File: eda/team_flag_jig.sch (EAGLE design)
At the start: 7 parts, among them J2 AVR_SPI_PRG_6PTH

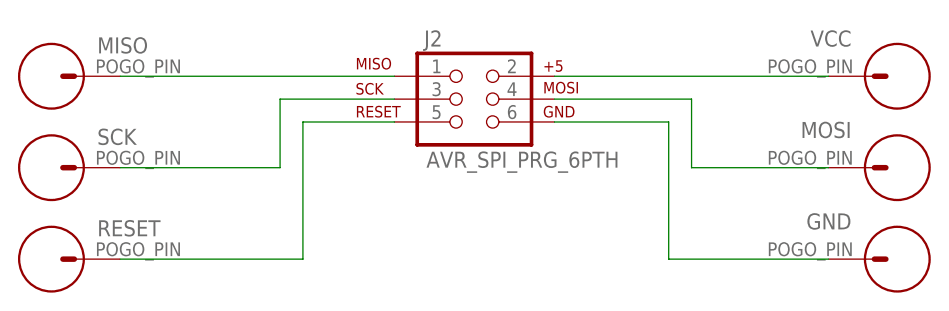
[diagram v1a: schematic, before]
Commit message: Ribboncable pinout fixed.
On battery_buzzer, smartsensor, and smartsensorPowered.
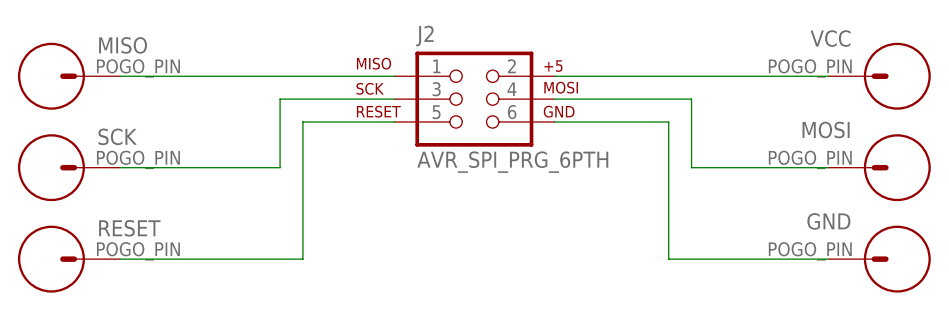
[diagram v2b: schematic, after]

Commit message: All jigs probe vias accessible after populating.
Also changed "VCC" signal name on jigs to "5V" to match boards.
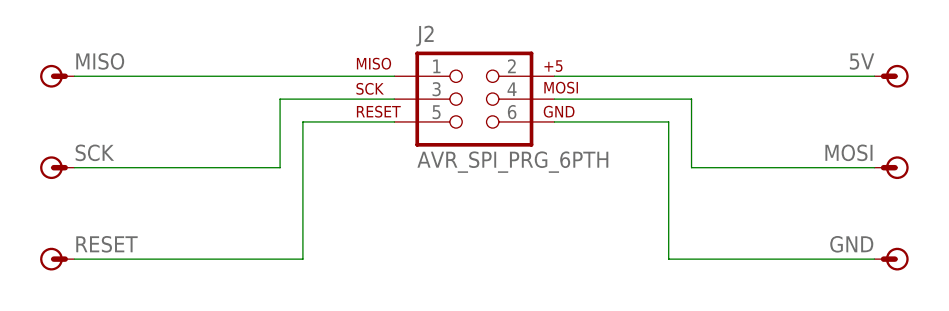
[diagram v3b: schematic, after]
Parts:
- renumbered VCC to 5V
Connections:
- net VCC renamed 5V
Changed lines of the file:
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@@
 <part name="SCK" library="pie" deviceset="POGO_PIN" device=""/>
 <part name="RESET" library="pie" deviceset="POGO_PIN" device=""/>
-<part name="VCC" library="pie" deviceset="POGO_PIN" device=""/>
+<part name="5V" library="pie" deviceset="POGO_PIN" device=""/>
 <part name="MOSI" library="pie" deviceset="POGO_PIN" device=""/>
 <part name="GND" library="pie" deviceset="POGO_PIN" device=""/>
@@
 </instance>
 <instance part="J2" gate="G$1" x="121.92" y="111.76"/>
-<instance part="MISO" gate="G$1" x="76.2" y="114.3"/>
-<instance part="SCK" gate="G$1" x="76.2" y="104.14"/>
-<instance part="RESET" gate="G$1" x="76.2" y="93.98"/>
-<instance part="VCC" gate="G$1" x="170.18" y="114.3" smashed="yes" rot="R180">
-<attribute name="NAME" x="165.1" y="119.38" size="1.778" layer="95" rot="R180"/>
+<instance part="MISO" gate="G$1" x="76.2" y="114.3" smashed="yes">
+<attribute name="VALUE" x="77.47" y="111.76" size="1.778" layer="96"/>
+<attribute name="NAME" x="78.74" y="115.062" size="1.778" layer="95"/>
+</instance>
+<instance part="SCK" gate="G$1" x="76.2" y="104.14" smashed="yes">
+<attribute name="VALUE" x="77.47" y="101.6" size="1.778" layer="96"/>
+<attribute name="NAME" x="78.74" y="104.902" size="1.778" layer="95"/>
+</instance>
+<instance part="RESET" gate="G$1" x="76.2" y="93.98" smashed="yes">
+<attribute name="VALUE" x="77.47" y="91.44" size="1.778" layer="96"/>
+<attribute name="NAME" x="78.74" y="94.742" size="1.778" layer="95"/>
+</instance>
+<instance part="5V" gate="G$1" x="170.18" y="114.3" smashed="yes" rot="R180">
+<attribute name="NAME" x="167.64" y="116.84" size="1.778" layer="95" rot="R180"/>
 <attribute name="VALUE" x="165.1" y="118.11" size="1.778" layer="96" rot="R180"/>
 </instance>
 <instance part="MOSI" gate="G$1" x="170.18" y="104.14" smashed="yes" rot="R180">
-<attribute name="NAME" x="165.1" y="109.22" size="1.778" layer="95" rot="R180"/>
+<attribute name="NAME" x="167.64" y="106.68" size="1.778" layer="95" rot="R180"/>
 <attribute name="VALUE" x="165.1" y="107.95" size="1.778" layer="96" rot="R180"/>
 </instance>
 <instance part="GND" gate="G$1" x="170.18" y="93.98" smashed="yes" rot="R180">
-<attribute name="NAME" x="165.1" y="99.06" size="1.778" layer="95" rot="R180"/>
+<attribute name="NAME" x="167.64" y="96.52" size="1.778" layer="95" rot="R180"/>
 <attribute name="VALUE" x="165.1" y="97.79" size="1.778" layer="96" rot="R180"/>
 </instance>
@@
 <wire x1="144.78" y1="109.22" x2="144.78" y2="93.98" width="0.1524" layer="91"/>
 <pinref part="GND" gate="G$1" pin="P$1"/>
-<wire x1="144.78" y1="93.98" x2="162.56" y2="93.98" width="0.1524" layer="91"/>
+<wire x1="144.78" y1="93.98" x2="167.64" y2="93.98" width="0.1524" layer="91"/>
 </segment>
 </net>
@@
 <wire x1="147.32" y1="111.76" x2="147.32" y2="104.14" width="0.1524" layer="91"/>
 <pinref part="MOSI" gate="G$1" pin="P$1"/>
-<wire x1="147.32" y1="104.14" x2="162.56" y2="104.14" width="0.1524" layer="91"/>
+<wire x1="147.32" y1="104.14" x2="167.64" y2="104.14" width="0.1524" layer="91"/>
 </segment>
 </net>
-<net name="VCC" class="0">
+<net name="5V" class="0">
 <segment>
 <pinref part="J2" gate="G$1" pin="2"/>
-<pinref part="VCC" gate="G$1" pin="P$1"/>
-<wire x1="132.08" y1="114.3" x2="162.56" y2="114.3" width="0.1524" layer="91"/>
+<pinref part="5V" gate="G$1" pin="P$1"/>
+<wire x1="132.08" y1="114.3" x2="167.64" y2="114.3" width="0.1524" layer="91"/>
 </segment>
 </net>
@@
 <wire x1="104.14" y1="109.22" x2="104.14" y2="93.98" width="0.1524" layer="91"/>
 <pinref part="RESET" gate="G$1" pin="P$1"/>
-<wire x1="104.14" y1="93.98" x2="83.82" y2="93.98" width="0.1524" layer="91"/>
+<wire x1="104.14" y1="93.98" x2="78.74" y2="93.98" width="0.1524" layer="91"/>
 </segment>
 </net>
@@
 <wire x1="101.6" y1="111.76" x2="101.6" y2="104.14" width="0.1524" layer="91"/>
 <pinref part="SCK" gate="G$1" pin="P$1"/>
-<wire x1="101.6" y1="104.14" x2="83.82" y2="104.14" width="0.1524" layer="91"/>
+<wire x1="101.6" y1="104.14" x2="78.74" y2="104.14" width="0.1524" layer="91"/>
 </segment>
 </net>
@@
 <segment>
 <pinref part="J2" gate="G$1" pin="1"/>
-<wire x1="114.3" y1="114.3" x2="83.82" y2="114.3" width="0.1524" layer="91"/>
+<wire x1="114.3" y1="114.3" x2="78.74" y2="114.3" width="0.1524" layer="91"/>
 <pinref part="MISO" gate="G$1" pin="P$1"/>
 </segment>
